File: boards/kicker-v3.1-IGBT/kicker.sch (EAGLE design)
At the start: 133 parts, among them J1 B2PS-VH(LF)(SN), J2 HFW8R-1ST, J3 B2PS-VH(LF)(SN), J4 B2PS-VH(LF)(SN), J5 2-PIN_2MM-H, J6 3-PIN_2MM-H, J7 !BTN_KCK_PRE_EXT, J8 !BTN_CHP_PRE_EXT, J9 !BTN_CHG_PRE_EXT, Q1 ATP302ATPAK, Q10 BSS806NSOT-23-3, Q2 IRFS4227, Q3 BSS127, Q4 BSS127, Q5 BSS127, Q6 BSS127, Q7 AOD1N60, U1 R-78E5.0-0.5, U2 15V, U3 LT3751FE, U4 AT32ATQFP44, U5 IX4427N, U6 MAX6817, U7 MAX6817

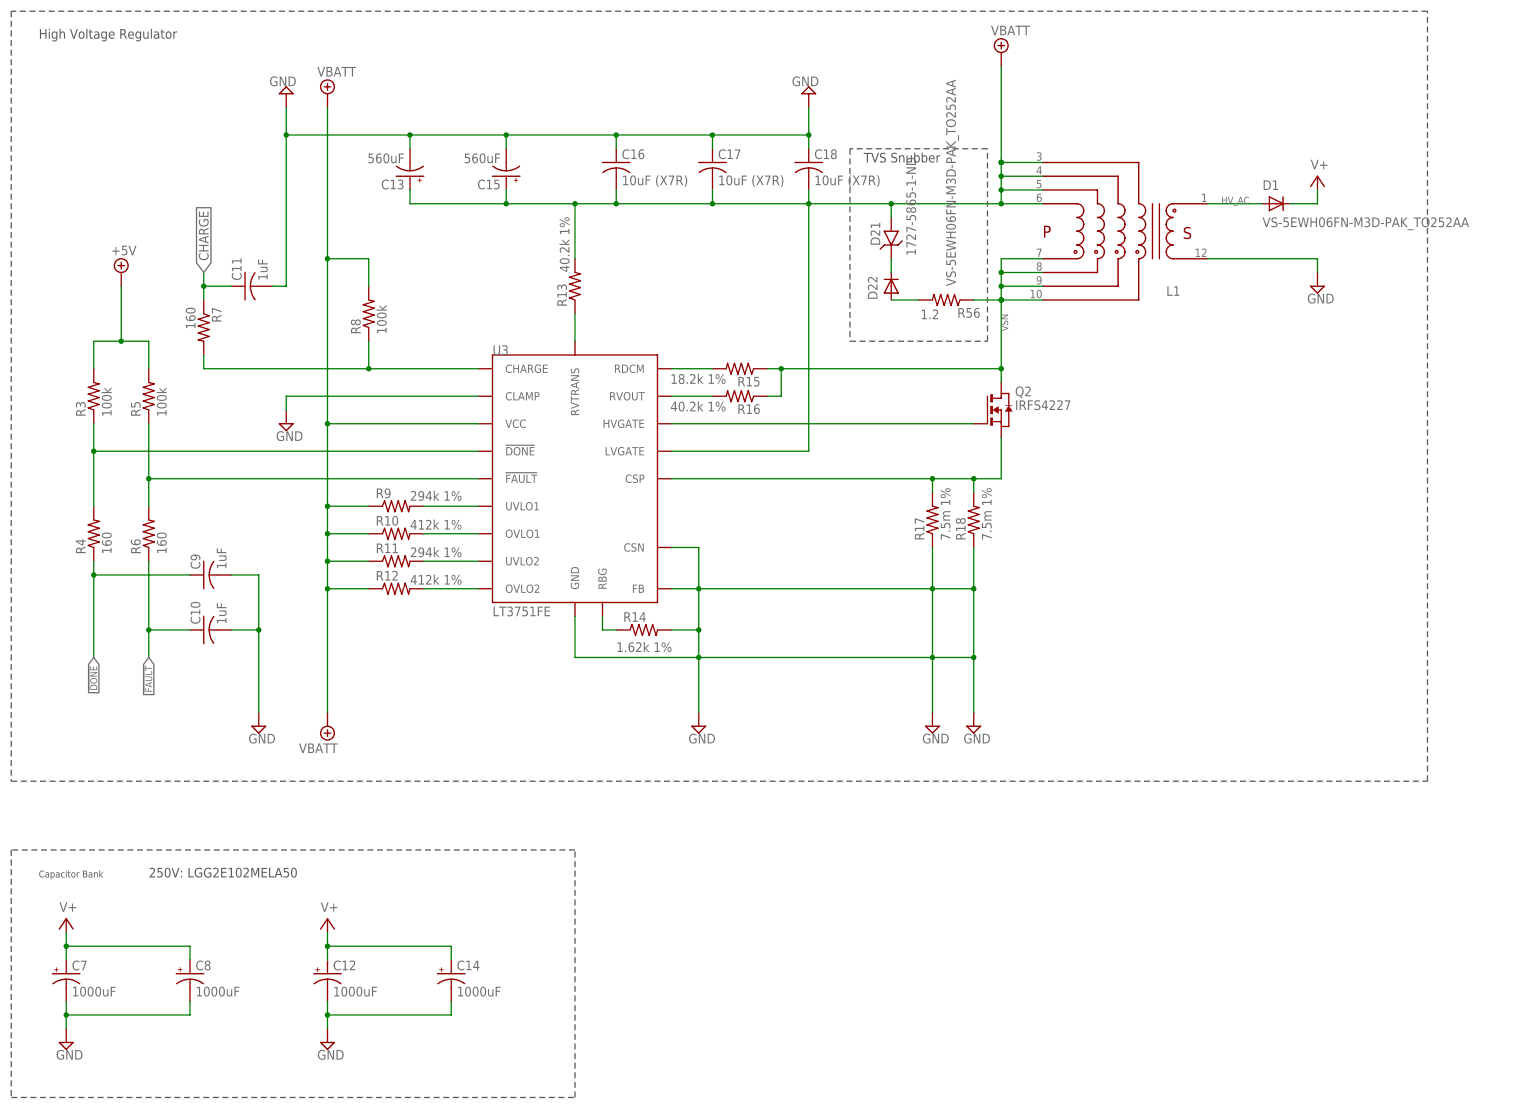
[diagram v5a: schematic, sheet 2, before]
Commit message: Added more tvs diodes and caps
Needs to be routed and checked
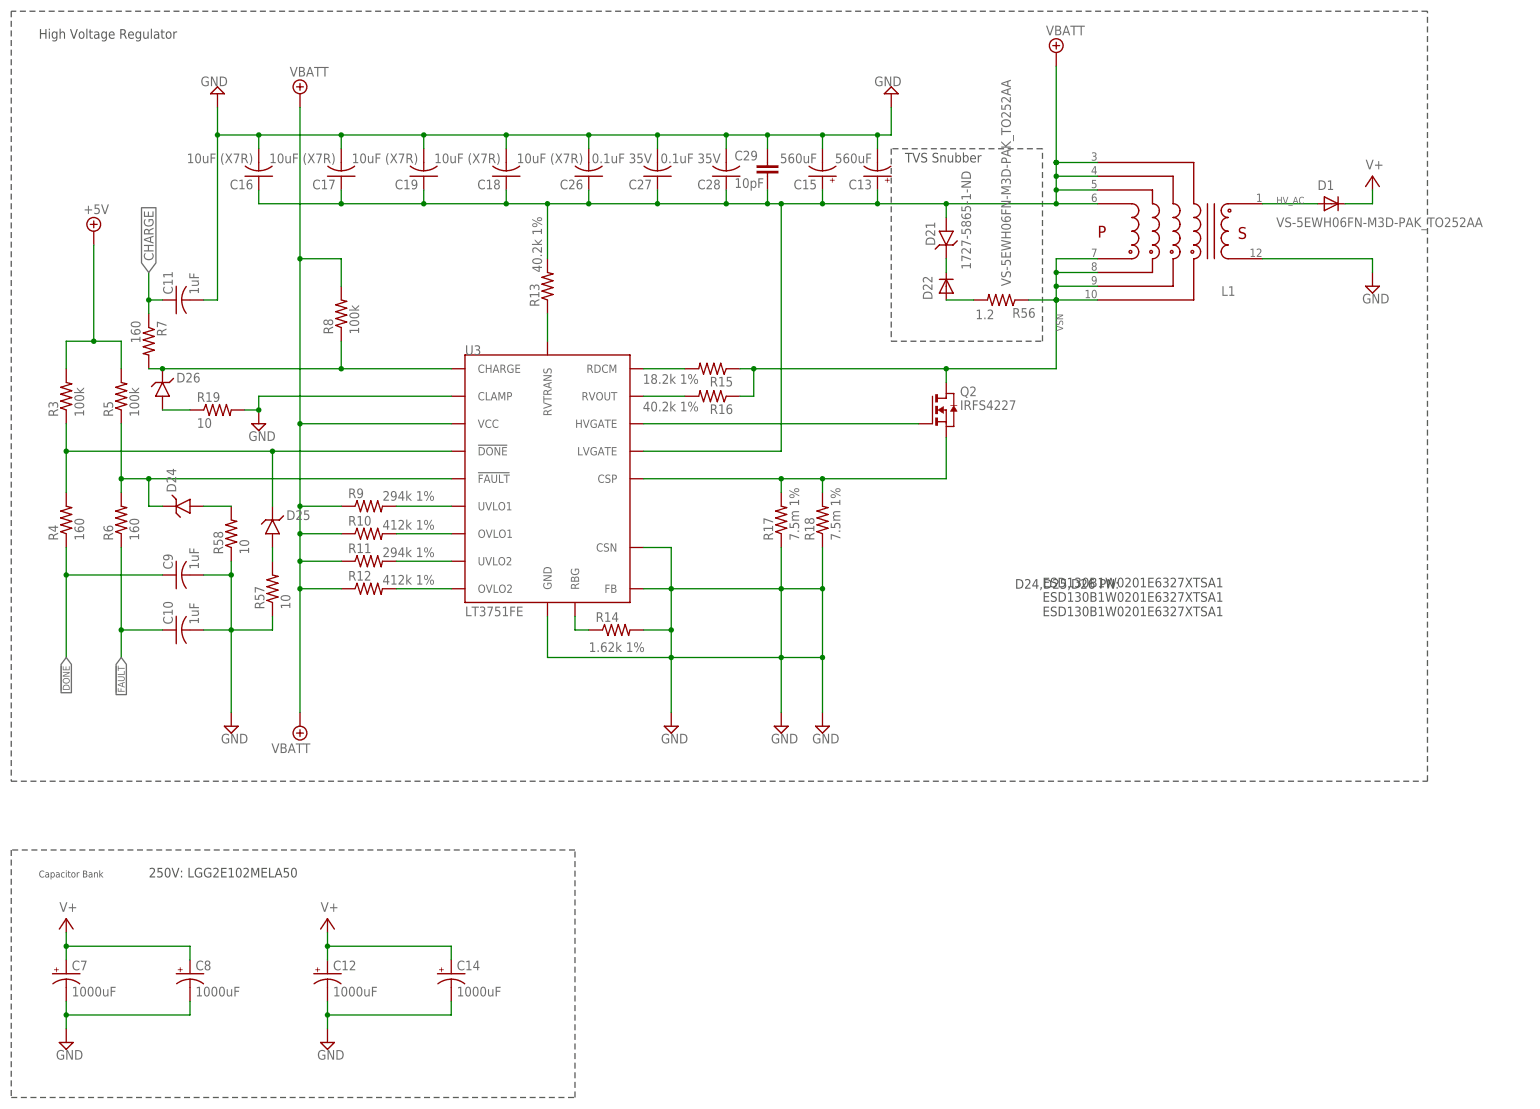
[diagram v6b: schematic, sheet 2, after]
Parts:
- added C19, C26: 10uF (X7R), rcl:C-USC1210
- added C27, C28: 0.1uF 35V, rcl:C-USC0603
- added C29: 10pF, SparkFun-Capacitors:10PF-50V-5%(0603)
- added D23: ESD130B1W0201E6327XTSA1, RoboJackets-Diodes:TVS0201
- added D24, D25, D26: (no value), RoboJackets-Diodes:TVS0201
- added R19, R57, R58, R59: 10, rcl:R-US_R0201
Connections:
- new net N$25: D23.A, R59.2
- new net N$31: D26.A, R19.1
- new net N$32: D25.A, R57.2
- new net N$33: D24.A, R58.2
- net !DONE_LPF: now also D25.C
- net !FAULT_LPF: now also D24.C
- net +5V: now also D23.C
- net CHARGE_LPF: now also D26.C
- net GND: now also C16.2, C17.2, C18.2, C19.2, C26.2, C27.2, C28.2, C29.1, R19.2, R57.1, R58.1, R59.1; no longer C16.1, C17.1, C18.1
- net VBATT: now also C16.1, C17.1, C18.1, C19.1, C26.1, C27.1, C28.1, C29.2; no longer C16.2, C17.2, C18.2
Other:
- note added: "D24,D25,D26 PN:"
- note added: "ESD130B1W0201E6327XTSA1 ESD130B1W0201E6327XTSA1 ESD130B1W0201E6327XTSA1"
- moved on the sheet: C10, C11, C13, C15, C16, C17, C18, C9, D1, D21, D22, L1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

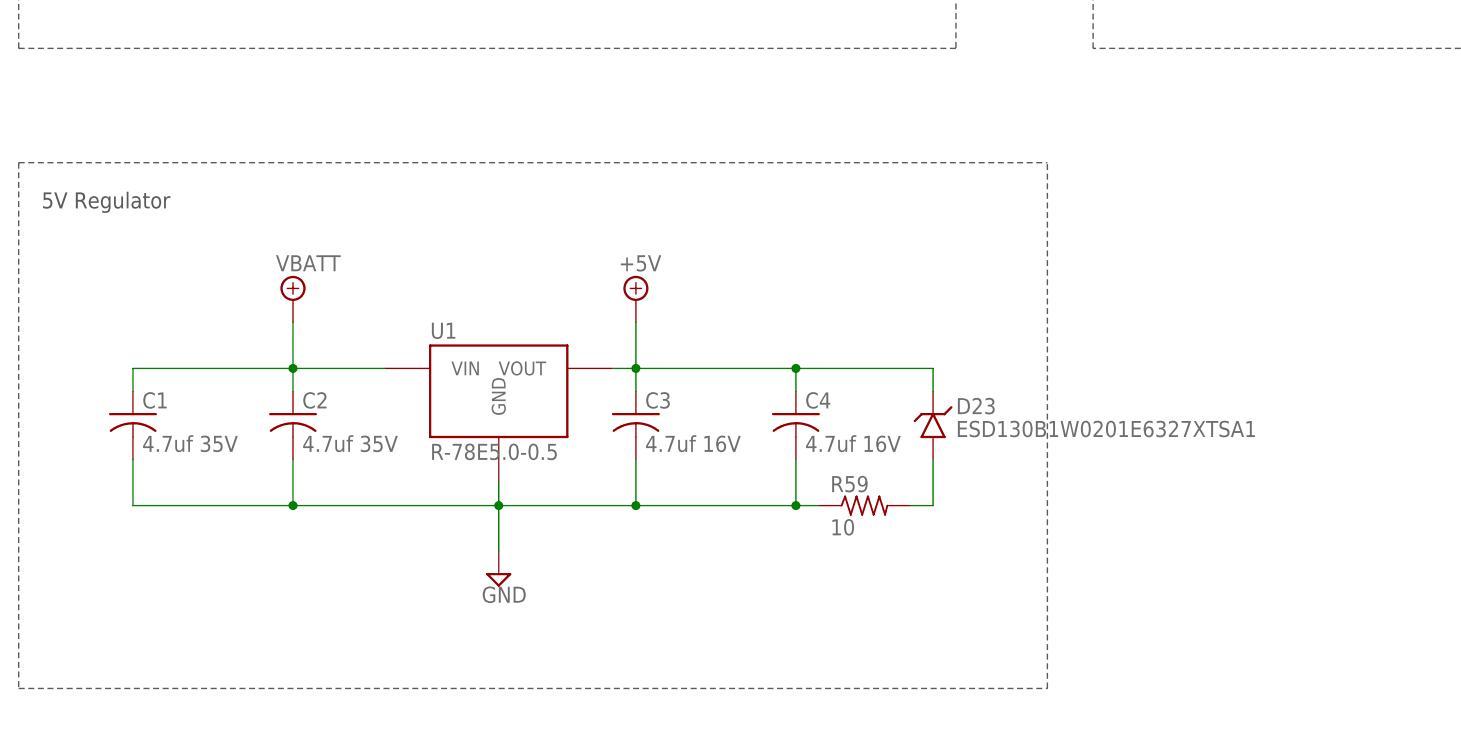
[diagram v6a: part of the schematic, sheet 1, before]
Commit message: replaced 5v buck, added FB resistor divider, more routing
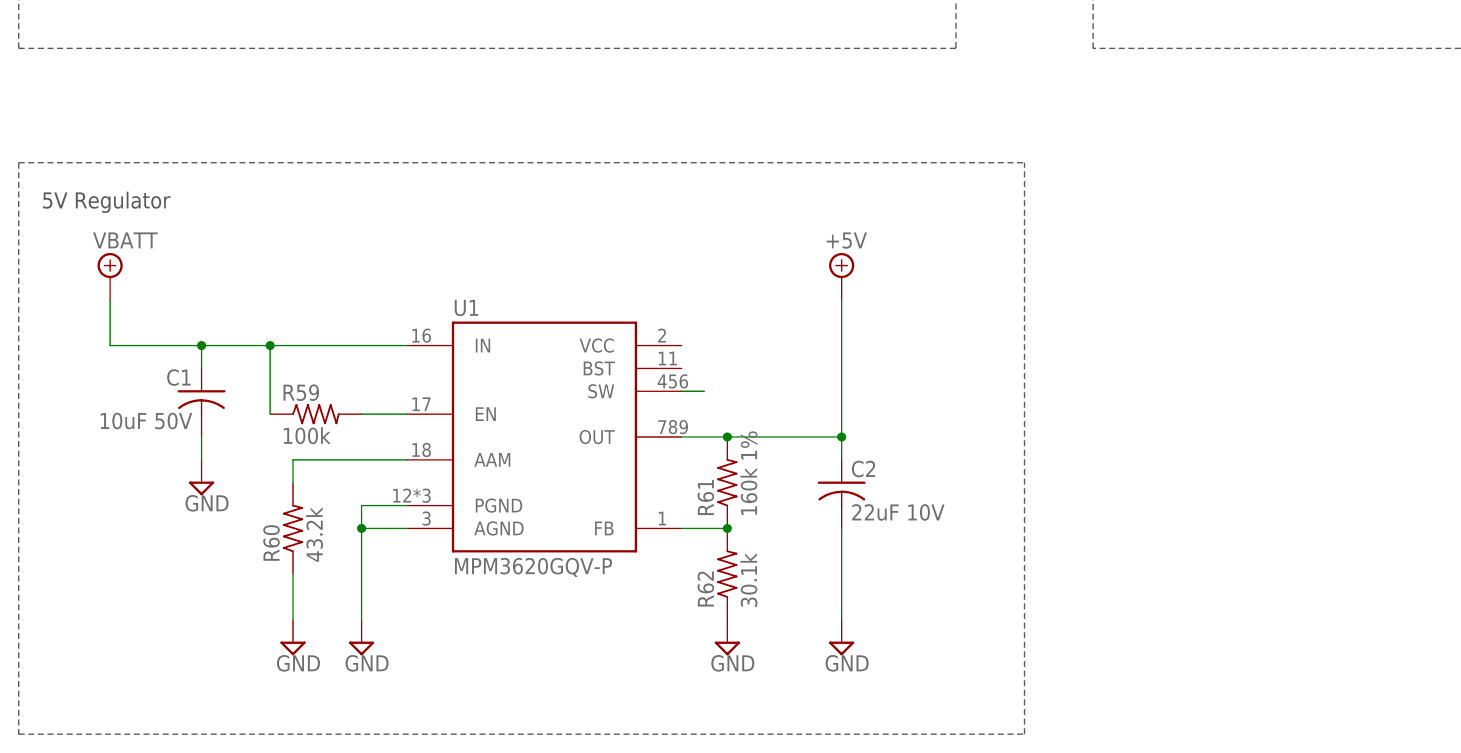
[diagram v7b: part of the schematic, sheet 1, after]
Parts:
- removed C3, C4: 4.7uf 16V, rcl:C-USC1210
- removed D23: ESD130B1W0201E6327XTSA1, RoboJackets-Diodes:TVS0201
- removed R19, R57, R58: 10, rcl:R-US_R0201
- added R60: 43.2k, rcl:R-US_R0603
- added R61: 160k 1%, rcl:R-US_R0402
- added R62: 30.1k, rcl:R-US_R0402
- added R63: 187k, rcl:R-US_R1206
- added R64: 931, rcl:R-US_R0805
- C1: value 4.7uf 35V -> 10uF 50V; device rcl:C-USC1210 -> rcl:C-USC1206
- C2: value 4.7uf 35V -> 22uF 10V; device rcl:C-USC1210 -> rcl:C-USC0603
- D21: value 1727-5865-1-ND -> (none)
- D24, D25, D26: device RoboJackets-Diodes:TVS0201 -> RoboJackets-Diodes:TVS0603
- R56: device resistor:R-US_M0805 -> resistor:R-US_R0805
- R59: value 10 -> 100k; device rcl:R-US_R0201 -> rcl:R-US_R0402
- U1: value R-78E5.0-0.5 -> MPM3620GQV-P; device RoboJackets-PowerICs:R-78E5.0-0.5 -> RoboJackets-PowerICs:MPM3620GQV-P
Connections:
- removed net N$25: D23.A, R59.2
- removed net N$31: D26.A, R19.1
- removed net N$32: D25.A, R57.2
- removed net N$33: D24.A, R58.2
- new net N$36: R63.2, R64.1, U3.FB
- new net REG-SW: U1.SW
- new net REG_AAM: R60.2, U1.AAM
- new net REG_EN: R59.2, U1.EN
- new net REG_FB: R61.1, R62.2, U1.FB
- net !DONE_LPF: now also D24.C; no longer D25.C
- net !FAULT_LPF: now also D25.C; no longer D24.C
- net +5V: now also C2.1, R61.2, U1.OUT; no longer C3.1, C4.1, D23.C, U1.VOUT
- net GND: now also D24.A, D25.A, D26.A, R60.1, R62.1, R64.2, R8.2, U1.AGND, U1.PGND; no longer C3.2, C4.2, R19.2, R57.1, R58.1, R59.1, U1.GND, U3.FB
- net V+: now also R63.1
- net VBATT: now also R59.1, U1.IN; no longer C2.1, R8.2, U1.VIN
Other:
- note added: "1727-5865-1-ND VS-5EWH06FN-M3D-PAK_TO252AA"
- note added: "D21,D22 PN:"
- note added: "PESD5V0C1USFYL PESD5V0C1USFYL PESD5V0C1USFYL"
- note removed: "ESD130B1W0201E6327XTSA1 ESD130B1W0201E6327XTSA1 ESD130B1W0201E6327XTSA1"
- moved on the sheet: C1, C2, D24, D26, R59

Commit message: Fixes to J5, ball/charge LEDs, routing
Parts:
- added D23: PESD5V0C1USFYL, RoboJackets-Diodes:TVS0603
- D3: value GREEN -> BLUE; device RoboJackets-LEDs:LED-SMD-GREEN -> RoboJackets-LEDs:LED-SMD-BLUE
- D5: value GREEN -> YELLOW; device RoboJackets-LEDs:LED-SMD-GREEN -> RoboJackets-LEDs:LED-SMD-YELLOW
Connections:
- net +5V: now also D23.C
- net GND: now also D23.A
- net N$19: now also J5.2; no longer J5.1
- net N$6: now also J5.1; no longer J5.2
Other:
- moved on the sheet: J5
